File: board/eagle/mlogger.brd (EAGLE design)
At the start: 59.4 x 33.3 mm, 42 parts, among them J1 MICROSD-9P, SW1 SS-12D00G3, SW2 TVAF06-A020B-R, SW3 TVAF06-A020B-R

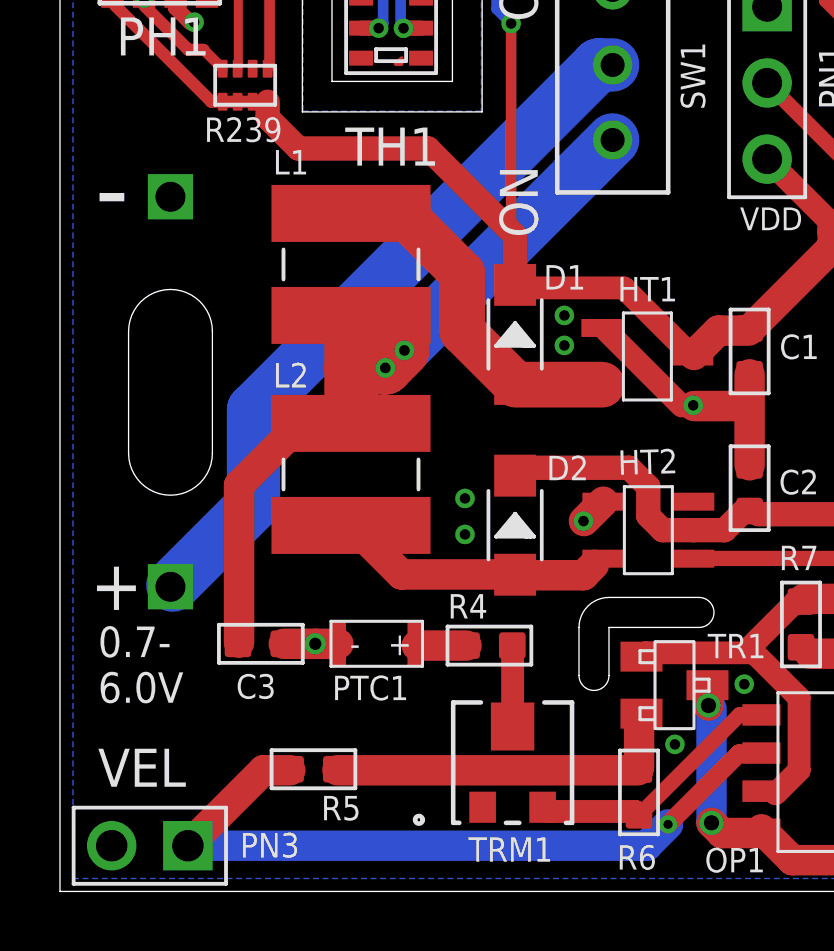
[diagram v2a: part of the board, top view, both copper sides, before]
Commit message: 温度補償サーミスタの位置改良
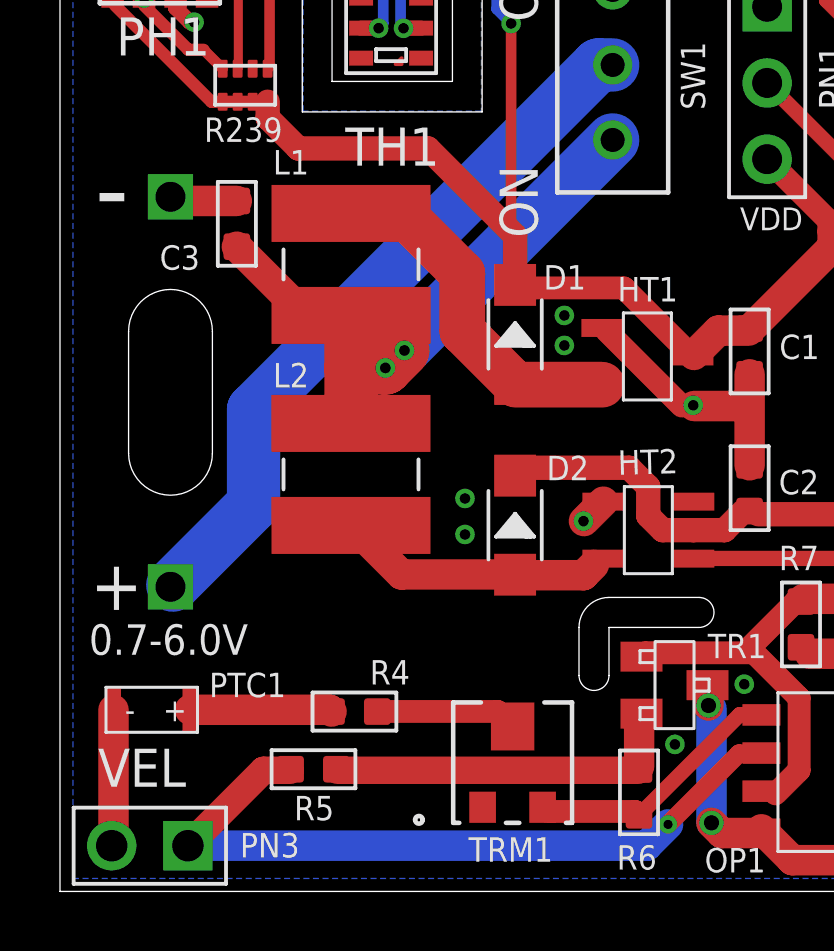
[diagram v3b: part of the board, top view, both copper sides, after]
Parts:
- moved C3 14.0 mm to (5.90, 22.3), turned to 0 degrees
- moved PTC1 7.82 mm to (1.78, 6.05)
- moved R4 5.01 mm to (9.81, 6.00)
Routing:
- net P$11: track 26.3 -> 21.1 mm
- net GND: track 53.3 -> 58.2 mm, vias 19 -> 18
- net N$28: track 1.74 -> 4.74 mm
- net N$1: track 2.70 -> 4.72 mm
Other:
- board text added: "0.7-6.0V"
- board text removed: "0.7- 6.0V"
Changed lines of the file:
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@@
 <setting verticaltext="up"/>
 </settings>
-<grid distance="0.1" unitdist="mm" unit="mm" style="lines" multiple="1" display="yes" altdistance="1" altunitdist="mil" altunit="mil"/>
+<grid distance="3.93700787" unitdist="mil" unit="mil" style="lines" multiple="1" display="yes" altdistance="1" altunitdist="mil" altunit="mil"/>
 <layers>
 <layer number="1" name="Top" color="4" fill="1" visible="yes" active="yes"/>
@@
 <text x="1.166" y="22.188" size="2.54" layer="25">-</text>
 <text x="1.0152" y="9.3832" size="1.6764" layer="25">+</text>
-<text x="1.266" y="6.288" size="1.016" layer="25" font="vector">0.7-
-6.0V</text>
+<text x="0.966" y="7.888" size="1.016" layer="25" font="vector">0.7-6.0V</text>
 <polygon width="0.0762" layer="21">
 <vertex x="57.1246" y="31.242"/>
@@
 <element name="D2" library="Seeed-Diode" package="SOD-123" value="20V-1A" x="15.17" y="12.208" smashed="yes" rot="R90">
 <attribute name="MPN" value="B5819W" x="15.17" y="12.208" size="1.778" layer="27" rot="R90" display="off"/>
+<attribute name="NAME" x="15.805" y="11.319" size="0.381" layer="33" ratio="10" rot="R90"/>
 <attribute name="NAME" x="17.629" y="14.519" size="0.8128" layer="25" ratio="11" rot="R180"/>
-<attribute name="NAME" x="15.805" y="11.319" size="0.381" layer="33" ratio="10" rot="R90"/>
 <attribute name="VALUE" x="17.202" y="10.303" size="0.889" layer="27" font="vector" ratio="11" rot="R90"/>
 </element>
@@
 <attribute name="NAME" x="21.4874" y="0.6356" size="0.8128" layer="25"/>
 </element>
-<element name="PTC1" library="MyParts" package="TFPT1206" value="TFPT1206" x="9.2832" y="8.255" smashed="yes">
-<attribute name="NAME" x="9.072" y="6.3754" size="0.8128" layer="25"/>
+<element name="PTC1" library="MyParts" package="TFPT1206" value="TFPT1206" x="1.7832" y="6.055" smashed="yes">
+<attribute name="NAME" x="4.972" y="6.4754" size="0.8128" layer="25"/>
 </element>
 <element name="BB1" library="MyParts" package="BH321" value="BH321" x="59.182" y="0.254" smashed="yes" rot="MR0">
@@
 <attribute name="NAME" x="12.6448" y="25.4628" size="1.27" layer="25" rot="R180"/>
 </element>
-<element name="C3" library="MyParts" package="C0603" package3d_urn="urn:adsk.eagle:package:8004287/1" value="" x="6.6952" y="8.254" smashed="yes" rot="R270">
-<attribute name="NAME" x="5.865" y="6.4268" size="0.8128" layer="25" ratio="11"/>
-<attribute name="NAME" x="7.9652" y="8.508" size="0.635" layer="33" ratio="10" rot="R180"/>
-<attribute name="VALUE" x="7.9652" y="9.8415" size="0.635" layer="27" ratio="10" rot="R180"/>
+<element name="C3" library="MyParts" package="C0603" package3d_urn="urn:adsk.eagle:package:8004287/1" value="" x="5.8952" y="22.254" smashed="yes">
+<attribute name="NAME" x="3.3224" y="20.7238" size="0.8128" layer="25" ratio="11"/>
+<attribute name="NAME" x="5.6412" y="23.524" size="0.635" layer="33" ratio="10" rot="R270"/>
+<attribute name="VALUE" x="4.3077" y="23.524" size="0.635" layer="27" ratio="10" rot="R270"/>
 </element>
 <element name="C2" library="MyParts" package="C0603" package3d_urn="urn:adsk.eagle:package:8004287/1" value="" x="22.987" y="13.4412" smashed="yes" rot="R180">
@@
 <attribute name="VALUE" x="56.0125" y="32.27" size="0.635" layer="27" ratio="10" rot="R270"/>
 </element>
-<element name="R4" library="MyParts" package="R0603" package3d_urn="urn:adsk.eagle:package:8004941/1" value="" x="14.3146" y="8.1952" smashed="yes" rot="R90">
-<attribute name="NAME" x="12.9278" y="9.098" size="0.8128" layer="25" ratio="11"/>
-<attribute name="VALUE" x="15.9196" y="9.6302" size="0.635" layer="27" ratio="10" rot="R180"/>
+<element name="R4" library="MyParts" package="R0603" package3d_urn="urn:adsk.eagle:package:8004941/1" value="" x="9.8146" y="5.9952" smashed="yes" rot="R90">
+<attribute name="NAME" x="10.3278" y="6.898" size="0.8128" layer="25" ratio="11"/>
+<attribute name="VALUE" x="11.4196" y="7.4302" size="0.635" layer="27" ratio="10" rot="R180"/>
 </element>
 <element name="R5" library="MyParts" package="R0603" package3d_urn="urn:adsk.eagle:package:8004941/1" value="" x="8.4492" y="4.0732" smashed="yes" rot="R90">
-<attribute name="NAME" x="8.7032" y="2.3714" size="0.8128" layer="25" ratio="11"/>
+<attribute name="NAME" x="7.8032" y="2.3714" size="0.8128" layer="25" ratio="11"/>
 <attribute name="VALUE" x="10.0542" y="5.5082" size="0.635" layer="27" ratio="10" rot="R180"/>
 </element>
@@
 <wire x1="37.8968" y1="20.9296" x2="38.608" y2="21.6408" width="0.254" layer="1"/>
 <wire x1="37.8968" y1="20.9296" x2="37.846" y2="20.9042" width="0.254" layer="1"/>
-<wire x1="7.361053125" y1="8.1534" x2="7.4572" y2="8.254" width="0.254" layer="1"/>
 <wire x1="55.6768" y1="11.4808" x2="55.6768" y2="10.5664" width="0.762" layer="1"/>
 <wire x1="55.6768" y1="10.5664" x2="55.6462" y2="10.4892" width="0.254" layer="1"/>
@@
 <wire x1="56.4866" y1="1.8258" x2="56.5308" y2="1.8258" width="0.254" layer="1"/>
 <wire x1="56.5308" y1="1.8258" x2="57.1754" y2="2.4704" width="1.016" layer="1"/>
-<wire x1="7.4572" y1="8.254" x2="8.509" y2="8.254" width="1.016" layer="1"/>
-<wire x1="8.509" y1="8.254" x2="9.2822" y2="8.254" width="1.016" layer="1"/>
-<wire x1="9.2822" y1="8.254" x2="9.2832" y2="8.255" width="0.254" layer="1"/>
-<via x="8.509" y="8.254" extent="1-16" drill="0.4064"/>
 <polygon width="0.0254" layer="16">
 <vertex x="0.4318" y="32.8422"/>
@@
 <wire x1="37.846" y1="20.9042" x2="37.3" y2="20.3582" width="0.254" layer="1"/>
 <wire x1="37.3" y1="20.3582" x2="37.3" y2="20.1" width="0.254" layer="1"/>
+<wire x1="5.8952" y1="23.016" x2="3.82" y2="23.016" width="1.016" layer="1"/>
+<wire x1="3.82" y1="23.016" x2="3.682" y2="23.154" width="1.016" layer="1"/>
+<wire x1="1.724" y1="1.524" x2="1.7832" y2="1.5832" width="1.016" layer="1"/>
+<wire x1="1.7832" y1="6.055" x2="1.7832" y2="1.5832" width="1.016" layer="1"/>
 </signal>
 <signal name="VDD" class="2">
@@
 <contactref element="C3" pad="2"/>
 <contactref element="SW1" pad="P$1"/>
-<wire x1="5.969" y1="13.5382" x2="5.969" y2="8.2898" width="1.016" layer="1"/>
-<wire x1="5.9332" y1="8.254" x2="5.969" y2="8.2898" width="0.762" layer="1"/>
-<wire x1="7.9756" y1="15.5448" x2="5.969" y2="13.5382" width="1.016" layer="1"/>
 <wire x1="10.8344" y1="17.4612" x2="18.4224" y2="25.0492" width="1.778" layer="16"/>
 <wire x1="10.8344" y1="17.4612" x2="10.8458" y2="17.4498" width="0.254" layer="16"/>
 <via x="10.8458" y="17.4498" extent="1-16" drill="0.3556"/>
 <wire x1="9.7" y1="15.6" x2="9.7" y2="17.4498" width="1.778" layer="1"/>
-<wire x1="9.7" y1="15.6" x2="9.6448" y2="15.5448" width="0.254" layer="1"/>
-<wire x1="9.6448" y1="15.5448" x2="7.9756" y2="15.5448" width="0.254" layer="1"/>
 <wire x1="10.8458" y1="17.4498" x2="9.7" y2="17.4498" width="1.778" layer="1"/>
 <wire x1="9.7" y1="17.4498" x2="9.7" y2="19.2" width="1.778" layer="1"/>
@@
 <wire x1="10.8458" y1="17.4498" x2="11.43" y2="18.034" width="1.778" layer="1"/>
 <wire x1="11.43" y1="18.034" x2="11.4808" y2="18.034" width="0.254" layer="1"/>
+<wire x1="5.8952" y1="21.492" x2="8.1872" y2="19.2" width="1.016" layer="1"/>
+<wire x1="8.1872" y1="19.2" x2="9.7" y2="19.2" width="0.254" layer="1"/>
 </signal>
 <signal name="P$2" class="2">
@@
 <contactref element="R6" pad="2"/>
 <wire x1="19.3" y1="4.062" x2="19.2766" y2="4.0386" width="0.762" layer="1"/>
-<wire x1="19.2766" y1="4.0386" x2="9.2458" y2="4.0386" width="1.016" layer="1"/>
+<wire x1="19.2766" y1="4.0386" x2="9.2458" y2="4.0386" width="0.9144" layer="1"/>
 <wire x1="9.2112" y1="4.0732" x2="9.2458" y2="4.0386" width="0.254" layer="1"/>
 <wire x1="19.304" y1="4.1656" x2="19.304" y2="5.8928" width="1.016" layer="1"/>
@@
 <contactref element="PN3" pad="1"/>
 <contactref element="R5" pad="1"/>
-<wire x1="6.7818" y1="4.0386" x2="7.67774375" y2="4.0386" width="1.016" layer="1"/>
-<wire x1="4.2672" y1="1.524" x2="6.7818" y2="4.0386" width="1.016" layer="1"/>
+<wire x1="6.7818" y1="4.0386" x2="7.67774375" y2="4.0386" width="0.9144" layer="1"/>
+<wire x1="4.2672" y1="1.524" x2="6.7818" y2="4.0386" width="0.9144" layer="1"/>
 <wire x1="7.67774375" y1="4.0386" x2="7.6872" y2="4.0732" width="0.254" layer="1"/>
 <wire x1="4.2672" y1="1.524" x2="4.264" y2="1.524" width="0.254" layer="1"/>
@@
 <contactref element="PTC1" pad="P$2"/>
 <contactref element="R4" pad="1"/>
-<wire x1="13.5526" y1="8.1952" x2="11.893" y2="8.1952" width="1.016" layer="1"/>
-<wire x1="11.8332" y1="8.255" x2="11.893" y2="8.1952" width="0.254" layer="1"/>
+<wire x1="9.0526" y1="5.9952" x2="8.9928" y2="6.055" width="1.016" layer="1"/>
+<wire x1="8.9928" y1="6.055" x2="4.3332" y2="6.055" width="1.016" layer="1"/>
 </signal>
 <signal name="P$7" class="2">
@@
 <contactref element="TRM1" pad="2"/>
 <contactref element="R4" pad="2"/>
-<wire x1="15.0766" y1="8.1952" x2="15.0876" y2="8.1842" width="0.762" layer="1"/>
-<wire x1="15.0876" y1="8.1842" x2="15.0876" y2="5.4991" width="0.762" layer="1"/>
+<wire x1="14.5876" y1="5.9991" x2="10.5805" y2="5.9991" width="0.762" layer="1"/>
+<wire x1="10.5766" y1="5.9952" x2="10.5805" y2="5.9991" width="0.762" layer="1"/>
+<wire x1="15.0876" y1="5.4991" x2="14.5876" y2="5.9991" width="0.762" layer="1"/>
 </signal>
 <signal name="N$9">

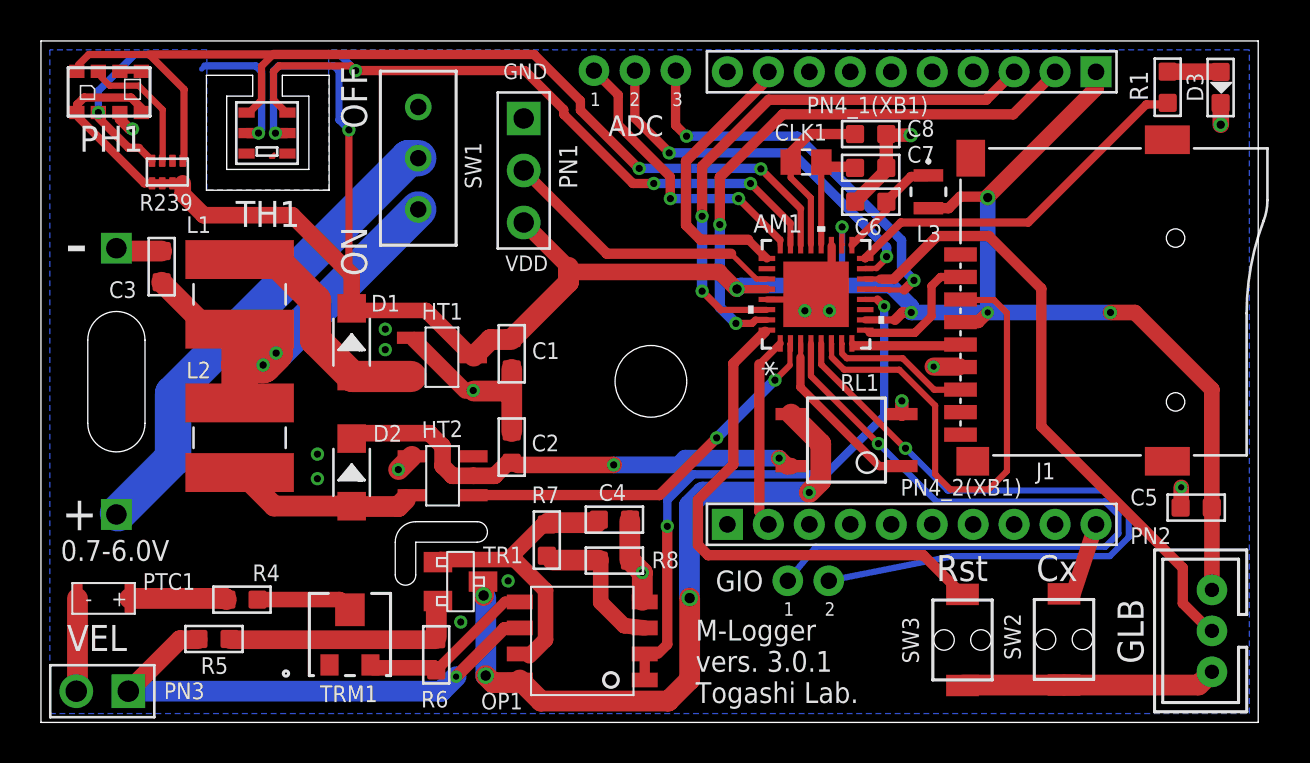
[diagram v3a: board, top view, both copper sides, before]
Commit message: 電源スイッチ位置の改良。 外部水晶発振子の設定修正。 風速センサ起動ピンの修正。 USARTのRXピンをプルアップ。 XBeeスリープのタイミングをmainメソッドに移行。
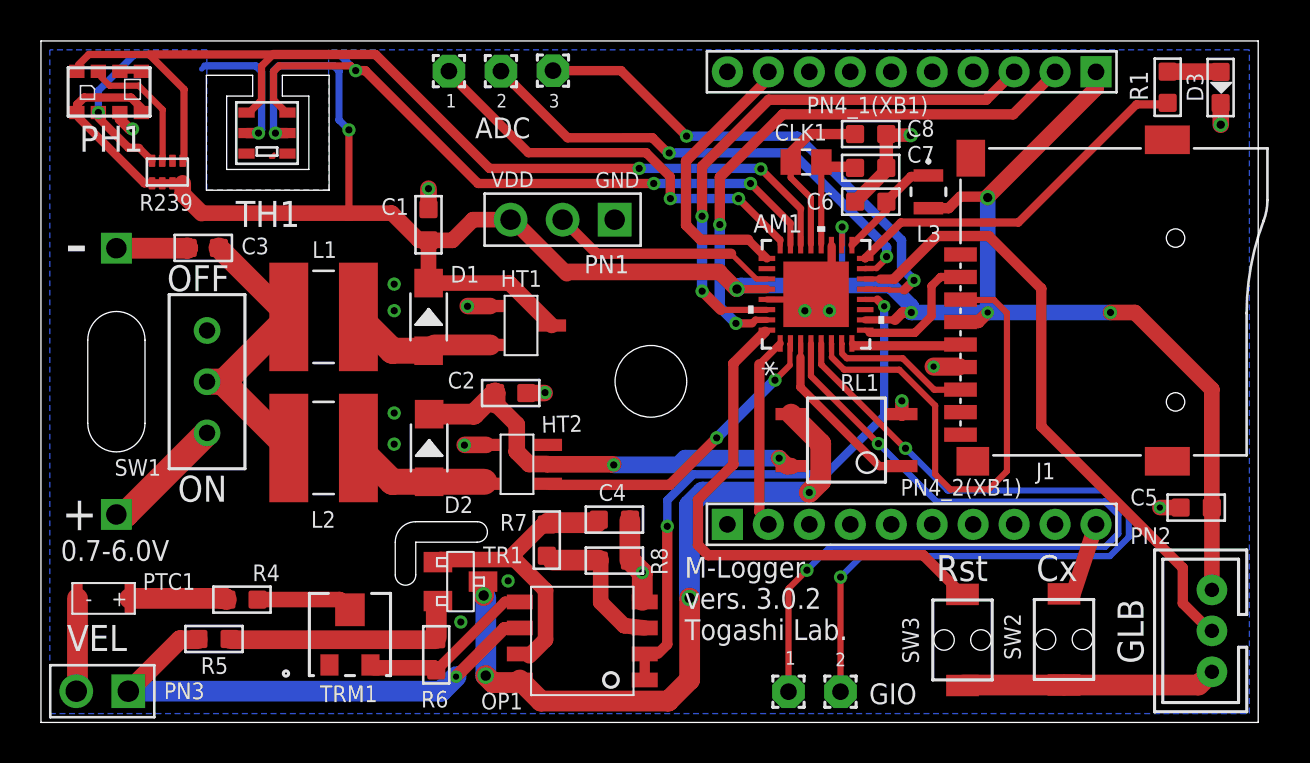
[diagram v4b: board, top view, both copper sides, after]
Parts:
- added PAD1, PAD2, PAD3, PAD4, PAD5: (no value), wirepad:1,6/0,8
- moved SW1 15.0 mm to (8.11, 16.6)
- moved C1 7.50 mm to (18.9, 24.3), turned to 180 degrees
- moved L1 4.24 mm to (13.8, 19.8), turned to 180 degrees
- moved HT1 4.16 mm to (22.4, 20.3)
- moved L2 4.13 mm to (13.8, 13.4), turned to 180 degrees
- moved D2 3.97 mm to (19.0, 13.4)
- moved D1 3.96 mm to (18.9, 19.8)
- moved HT2 3.68 mm to (24.2, 11.7)
- moved PN1 3.06 mm to (25.5, 24.5), turned to 270 degrees
- moved C2 2.64 mm to (22.9, 16.1), turned to 90 degrees
- moved C3 2.23 mm to (7.93, 23.2), turned to 90 degrees
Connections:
- removed net VBT: BB1.V+, SW1.P$2
- new net N$14: BB1.V+, SW1.P$1
- net N$11: now also PAD1.1
- net N$12: now also PAD3.1
- net N$13: now also PAD4.1
- net N$8: now also PAD2.1
- net N$9: now also PAD5.1
- net P$11: now also SW1.P$2; no longer SW1.P$1
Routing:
- net VBT: track 23.8 -> 0.00 mm
- net N$9: track 14.2 -> 20.5 mm, vias 3 -> 2
- net N$14: track 0.00 -> 6.08 mm
- net GND: track 58.2 -> 52.4 mm, vias 18 -> 20
- net P$11: track 21.1 -> 15.4 mm, vias 2 -> 0
- net N$12: track 35.4 -> 40.7 mm
- net N$11: track 19.0 -> 24.2 mm, vias 3 -> 2
- net N$13: track 37.5 -> 42.6 mm
- net P$13: track 11.9 -> 7.24 mm
- net N$8: track 20.8 -> 25.3 mm, vias 3 -> 2
- net N$23: track 19.2 -> 15.3 mm
- net N$7: track 14.1 -> 11.2 mm
- net V5: track 23.6 -> 20.9 mm
- net P$10: track 9.30 -> 6.97 mm
- net VDD: track 127.2 -> 125.9 mm
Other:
- board text added: "M-Logger vers. 3.0.2 Togashi Lab."
- board text removed: "M-Logger vers. 3.0.1 Togashi Lab."
